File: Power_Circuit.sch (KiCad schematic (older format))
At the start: 34 parts, among them J1 Conn_01x09, J2 Conn_01x04, SW1 SW_Push, SW2 SW_STARTER, U1 B_Plug_Battery_In, U10 DSN2596, U11 B_Plug_12v_Motor1, U12 B_Plug_12v_Motor2, U13 B_Plug_5v_Actuator, U2 DSN2596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

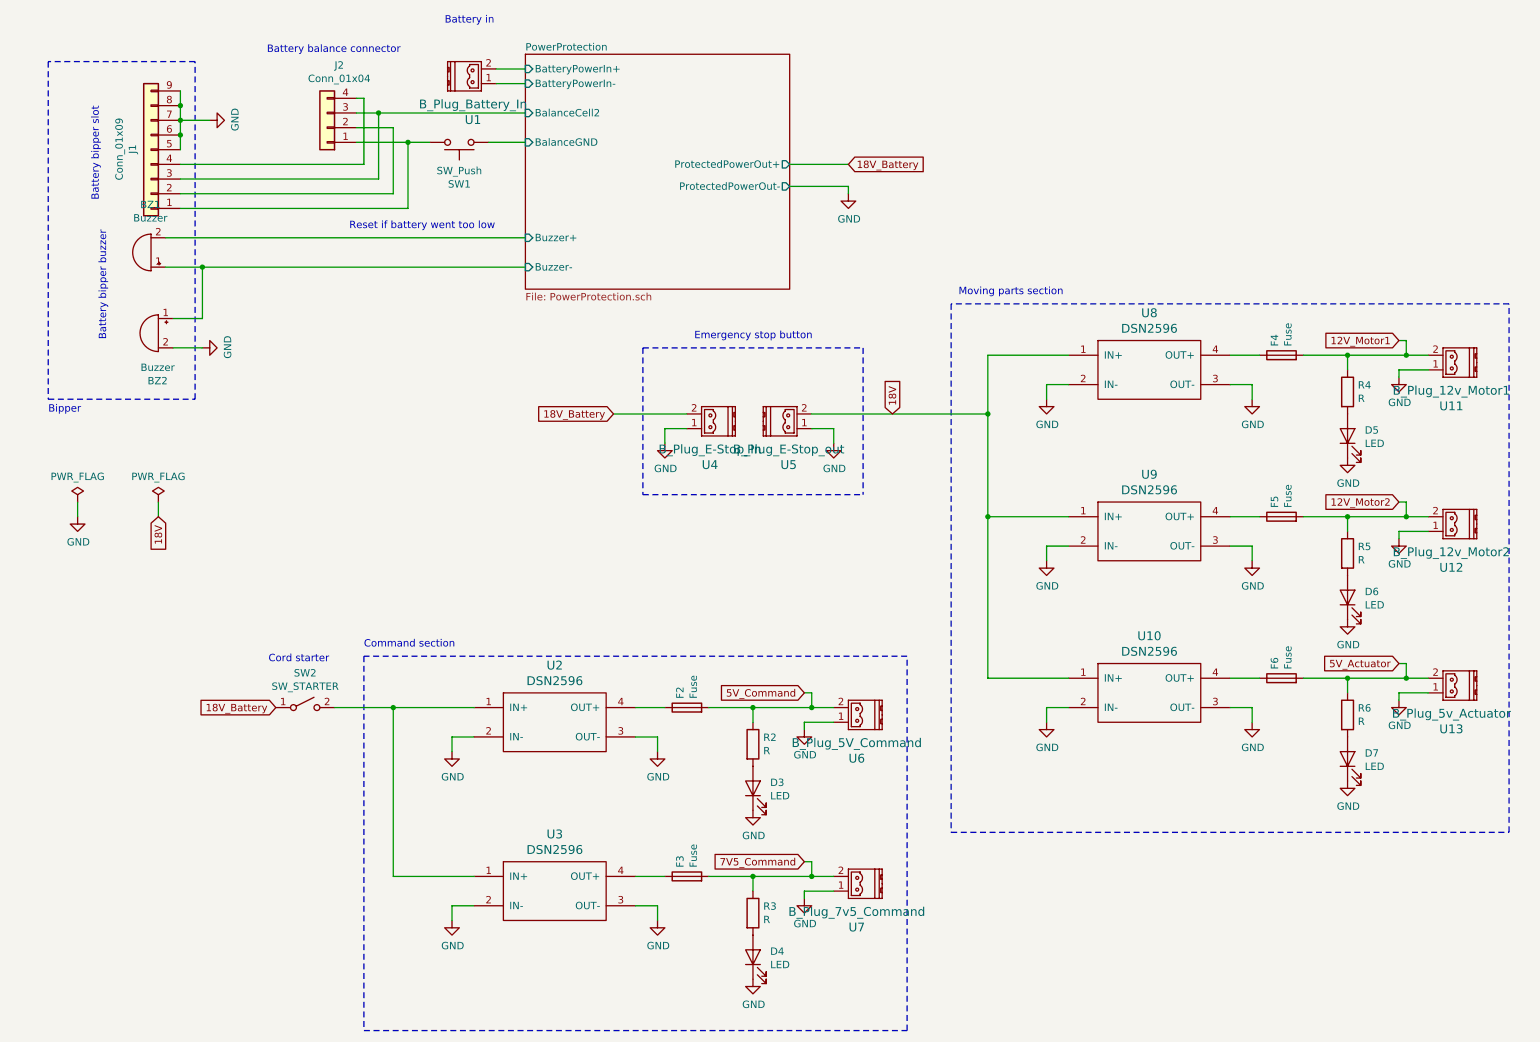
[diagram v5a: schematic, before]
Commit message: Avec regul moteur et texte sur autre couche
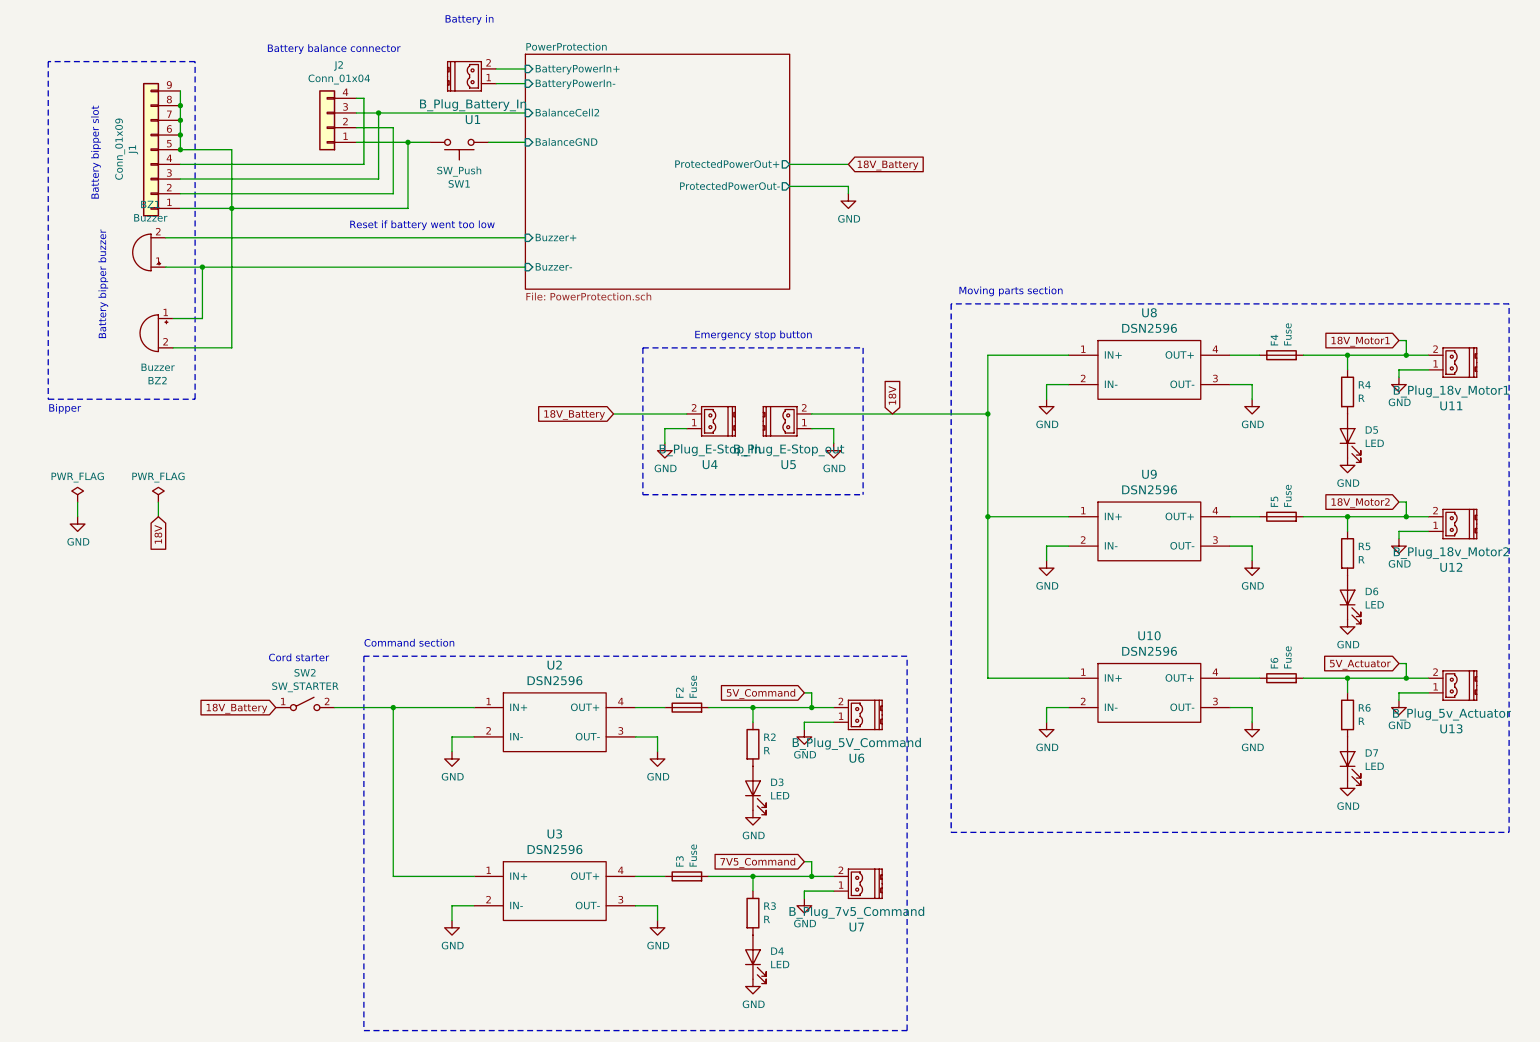
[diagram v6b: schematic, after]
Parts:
- U11: value B_Plug_12v_Motor1 -> B_Plug_18v_Motor1
- U12: value B_Plug_12v_Motor2 -> B_Plug_18v_Motor2
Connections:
- net GND: no longer BZ2.2 (+), J1.5 (Pin_5), J1.6 (Pin_6), J1.7 (Pin_7), J1.8 (Pin_8), J1.9 (Pin_9)
- net at J1.1 (Pin_1), J2.1 (Pin_1), SW1.2: now also BZ2.2 (+), J1.5 (Pin_5), J1.6 (Pin_6), J1.7 (Pin_7), J1.8 (Pin_8), J1.9 (Pin_9)
- net 12V_Motor1 renamed 18V_Motor1
- net 12V_Motor2 renamed 18V_Motor2
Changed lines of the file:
@@
 	6350 3600 6200 3600
-$Comp
-L dsn2596:DSN2596 U8
-U 1 1 5F54DB3F
-P 8500 3200
-F 0 "U8" H 8500 3587 60  0000 C CNN
-F 1 "DSN2596" H 8500 3481 60  0000 C CNN
-F 2 "DC_DC_LM2596_small:DC_DC_LM2596_small" H 8500 3200 60  0001 C CNN
-F 3 "" H 8500 3200 60  0000 C CNN
-	1    8500 3200
-	1    0    0    -1
-$EndComp
 $Comp
 L Device:R R4
@@
 $EndComp
 Wire Wire Line
-	9250 3100 9050 3100
-Wire Wire Line
 	9850 3100 9550 3100
 Connection ~ 9850 3100
-$Comp
-L power:GND #PWR018
-U 1 1 5F55577A
-P 9200 3400
-F 0 "#PWR018" H 9200 3150 50  0001 C CNN
-F 1 "GND" H 9205 3227 50  0000 C CNN
-F 2 "" H 9200 3400 50  0001 C CNN
-F 3 "" H 9200 3400 50  0001 C CNN
-	1    9200 3400
-	1    0    0    -1
-$EndComp
 $Comp
 L power:GND #PWR024
@@
 Wire Wire Line
 	10200 3200 10400 3200
-Wire Wire Line
-	9200 3400 9200 3300
-Wire Wire Line
-	9200 3300 9050 3300
 $Comp
 L 2:B_Plug_5mm U1
@@
 P 10500 3150
 F 0 "U11" H 10443 3447 60  0000 C CNN
-F 1 "B_Plug_12v_Motor1" H 10443 3341 60  0000 C CNN
+F 1 "B_Plug_18v_Motor1" H 10443 3341 60  0000 C CNN
 F 2 "Connector_Phoenix_MC:PhoenixContact_MCV_1,5_2-G-3.81_1x02_P3.81mm_Vertical" H 10500 3150 60  0001 C CNN
 F 3 "" H 10500 3150 60  0000 C CNN
 	1    10500 3150
 	-1   0    0    1
-$EndComp
-$Comp
-L power:GND #PWR015
-U 1 1 5F562803
-P 7800 3400
-F 0 "#PWR015" H 7800 3150 50  0001 C CNN
-F 1 "GND" H 7805 3227 50  0000 C CNN
-F 2 "" H 7800 3400 50  0001 C CNN
-F 3 "" H 7800 3400 50  0001 C CNN
-	1    7800 3400
-	1    0    0    -1
-$EndComp
-Wire Wire Line
-	7800 3400 7800 3300
-Wire Wire Line
-	7950 3300 7800 3300
-$Comp
-L dsn2596:DSN2596 U9
-U 1 1 5F568932
-P 8500 4300
-F 0 "U9" H 8500 4687 60  0000 C CNN
-F 1 "DSN2596" H 8500 4581 60  0000 C CNN
-F 2 "DC_DC_LM2596_small:DC_DC_LM2596_small" H 8500 4300 60  0001 C CNN
-F 3 "" H 8500 4300 60  0000 C CNN
-	1    8500 4300
-	1    0    0    -1
 $EndComp
 $Comp
@@
 $EndComp
 Wire Wire Line
-	9250 4200 9050 4200
-Wire Wire Line
 	9850 4200 9550 4200
 Connection ~ 9850 4200
-$Comp
-L power:GND #PWR019
-U 1 1 5F568954
-P 9200 4500
-F 0 "#PWR019" H 9200 4250 50  0001 C CNN
-F 1 "GND" H 9205 4327 50  0000 C CNN
-F 2 "" H 9200 4500 50  0001 C CNN
-F 3 "" H 9200 4500 50  0001 C CNN
-	1    9200 4500
-	1    0    0    -1
-$EndComp
 $Comp
 L power:GND #PWR025
@@
 Wire Wire Line
 	9850 4200 10250 4200
-Wire Wire Line
-	9200 4500 9200 4400
-Wire Wire Line
-	9200 4400 9050 4400
 $Comp
 L 2:B_Plug_5mm U12
@@
 P 10500 4250
 F 0 "U12" H 10443 4547 60  0000 C CNN
-F 1 "B_Plug_12v_Motor2" H 10443 4441 60  0000 C CNN
+F 1 "B_Plug_18v_Motor2" H 10443 4441 60  0000 C CNN
 F 2 "Connector_Phoenix_MC:PhoenixContact_MCV_1,5_2-G-3.81_1x02_P3.81mm_Vertical" H 10500 4250 60  0001 C CNN
 F 3 "" H 10500 4250 60  0000 C CNN
@@
 	-1   0    0    1
 $EndComp
-$Comp
-L power:GND #PWR016
-U 1 1 5F56896B
-P 7800 4500
-F 0 "#PWR016" H 7800 4250 50  0001 C CNN
-F 1 "GND" H 7805 4327 50  0000 C CNN
-F 2 "" H 7800 4500 50  0001 C CNN
-F 3 "" H 7800 4500 50  0001 C CNN
-	1    7800 4500
-	1    0    0    -1
-$EndComp
-Wire Wire Line
-	7800 4500 7800 4400
-Wire Wire Line
-	7950 4400 7800 4400
-Wire Wire Line
-	7950 4200 7400 4200
 $Comp
 L dsn2596:DSN2596 U10
@@
 Wire Wire Line
 	7950 5300 7400 5300
-Connection ~ 7400 4200
 Wire Wire Line
 	6200 3500 7400 3500
-Wire Wire Line
-	7400 3500 7400 4200
-Wire Wire Line
-	7400 4200 7400 5300
 Wire Notes Line
 	5050 4050 6550 4050
@@
 Wire Notes Line
 	5050 3050 6550 3050
-Text GLabel 10200 4100 0    50   Input ~ 0
-12V_Motor2
 Text GLabel 10200 5200 0    50   Input ~ 0
 5V_Actuator
@@
 Wire Wire Line
 	3900 5700 3750 5700
-Wire Wire Line
-	3900 5500 3350 5500
 Text GLabel 6150 5400 0    50   Input ~ 0
 5V_Command
@@
 Wire Notes Line
 	10950 6350 10950 2750
-Wire Notes Line
-	10950 2750 7150 2750
 Wire Notes Line
 	5050 3050 5050 4050
@@
 $EndComp
 Wire Wire Line
-	1900 2100 3450 2100
+	1900 2100 2250 2100
 Wire Wire Line
 	1900 1900 3250 1900
@@
 Wire Wire Line
 	6450 1950 6050 1950
-$Comp
-L power:GND #PWR02
-U 1 1 5FA54FE4
-P 2100 1500
-F 0 "#PWR02" H 2100 1250 50  0001 C CNN
-F 1 "GND" H 2105 1327 50  0000 C CNN
-F 2 "" H 2100 1500 50  0001 C CNN
-F 3 "" H 2100 1500 50  0001 C CNN
-	1    2100 1500
-	0    -1   -1   0
-$EndComp
-Wire Wire Line
-	2100 1500 1900 1500
 Wire Notes Line
 	1000 1100 1000 3400
@@
 Wire Wire Line
 	10250 3000 10250 3100
-Text GLabel 10200 3000 0    50   Input ~ 0
-12V_Motor1
 Wire Wire Line
 	10200 5400 10200 5450
@@
 Wire Wire Line
 	1200 4100 1200 4200
-Wire Wire Line
-	7950 3100 7400 3100
 $Comp
 L power:PWR_FLAG #FLG0102
@@
 Wire Wire Line
 	2050 2850 1850 2850
-$Comp
-L power:GND #PWR0103
-U 1 1 5FB650C4
-P 2050 3050
-F 0 "#PWR0103" H 2050 2800 50  0001 C CNN
-F 1 "GND" H 2055 2877 50  0000 C CNN
-F 2 "" H 2050 3050 50  0001 C CNN
-F 3 "" H 2050 3050 50  0001 C CNN
-	1    2050 3050
-	0    -1   -1   0
-$EndComp
-Wire Wire Line
-	2050 3050 1850 3050
 Wire Wire Line
 	2050 2850 2050 2500
@@
 Wire Wire Line
 	2050 2500 4250 2500
+Text GLabel 10200 4100 0    50   Input ~ 0
+18V_Motor2
+Text GLabel 10200 3000 0    50   Input ~ 0
+18V_Motor1
+Wire Wire Line
+	3900 5500 3350 5500
+Wire Wire Line
+	2250 2100 2250 3050
+Connection ~ 2250 2100
+Wire Wire Line
+	2250 2100 3450 2100
+Wire Wire Line
+	1850 3050 2250 3050
+Wire Wire Line
+	1900 1700 2250 1700
+Wire Wire Line
+	2250 1700 2250 2100
+Connection ~ 1900 1700
+Wire Wire Line
+	7400 3500 7400 4200
+Wire Notes Line
+	10950 2750 7150 2750
+$Comp
+L dsn2596:DSN2596 U9
+U 1 1 5FAB91D9
+P 8500 4300
+F 0 "U9" H 8500 4687 60  0000 C CNN
+F 1 "DSN2596" H 8500 4581 60  0000 C CNN
+F 2 "DC_DC_LM2596_small:DC_DC_LM2596_small" H 8500 4300 60  0001 C CNN
+F 3 "" H 8500 4300 60  0000 C CNN
+	1    8500 4300
+	1    0    0    -1
+$EndComp
+$Comp
+L power:GND #PWR0102
+U 1 1 5FAB91DF
+P 9200 4500
+F 0 "#PWR0102" H 9200 4250 50  0001 C CNN
+F 1 "GND" H 9205 4327 50  0000 C CNN
+F 2 "" H 9200 4500 50  0001 C CNN
+F 3 "" H 9200 4500 50  0001 C CNN
+	1    9200 4500
+	1    0    0    -1
+$EndComp
+Wire Wire Line
+	9200 4500 9200 4400
+Wire Wire Line
+	9200 4400 9050 4400
+$Comp
+L power:GND #PWR0103
+U 1 1 5FAB91E7
+P 7800 4500
+F 0 "#PWR0103" H 7800 4250 50  0001 C CNN
+F 1 "GND" H 7805 4327 50  0000 C CNN
+F 2 "" H 7800 4500 50  0001 C CNN
+F 3 "" H 7800 4500 50  0001 C CNN
+	1    7800 4500
+	1    0    0    -1
+$EndComp
+Wire Wire Line
+	7800 4500 7800 4400
+Wire Wire Line
+	7950 4400 7800 4400
+$Comp
+L dsn2596:DSN2596 U8
+U 1 1 5FABDC55
+P 8500 3200
+F 0 "U8" H 8500 3587 60  0000 C CNN
+F 1 "DSN2596" H 8500 3481 60  0000 C CNN
+F 2 "DC_DC_LM2596_small:DC_DC_LM2596_small" H 8500 3200 60  0001 C CNN
+F 3 "" H 8500 3200 60  0000 C CNN
+	1    8500 3200
+	1    0    0    -1
+$EndComp
+$Comp
+L power:GND #PWR0105
+U 1 1 5FABDC5B
+P 9200 3400
+F 0 "#PWR0105" H 9200 3150 50  0001 C CNN
+F 1 "GND" H 9205 3227 50  0000 C CNN
+F 2 "" H 9200 3400 50  0001 C CNN
+F 3 "" H 9200 3400 50  0001 C CNN
+	1    9200 3400
+	1    0    0    -1
+$EndComp
+Wire Wire Line
+	9200 3400 9200 3300
+Wire Wire Line
+	9200 3300 9050 3300
+$Comp
+L power:GND #PWR0107
+U 1 1 5FABDC63
+P 7800 3400
+F 0 "#PWR0107" H 7800 3150 50  0001 C CNN
+F 1 "GND" H 7805 3227 50  0000 C CNN
+F 2 "" H 7800 3400 50  0001 C CNN
+F 3 "" H 7800 3400 50  0001 C CNN
+	1    7800 3400
+	1    0    0    -1
+$EndComp
+Wire Wire Line
+	7800 3400 7800 3300
+Wire Wire Line
+	7950 3300 7800 3300
+Wire Wire Line
+	9250 3100 9050 3100
+Wire Wire Line
+	7950 3100 7400 3100
+Wire Wire Line
+	7950 4200 7400 4200
+Connection ~ 7400 4200
+Wire Wire Line
+	7400 4200 7400 5300
+Wire Wire Line
+	9250 4200 9050 4200
 $EndSCHEMATC

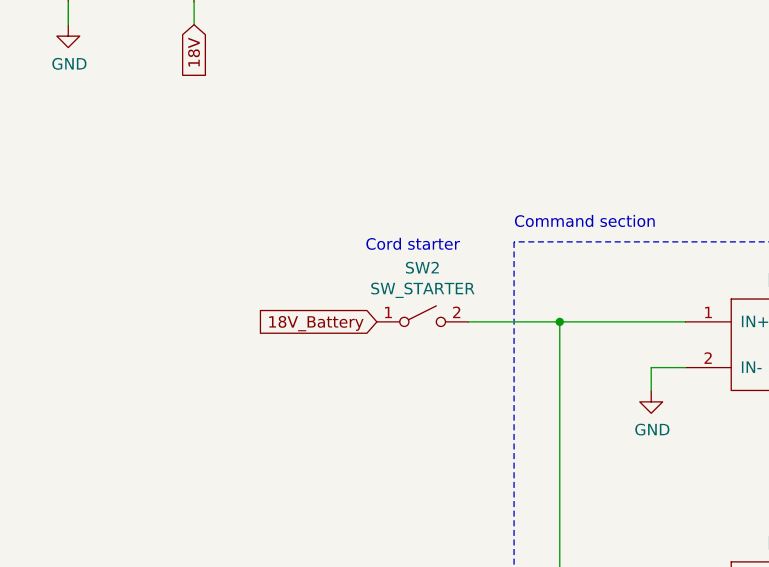
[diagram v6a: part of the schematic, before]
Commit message: Ajout BOM, suppression tirette, correction silk, correction des plans pour meilleur refroidissement du transistor notamment
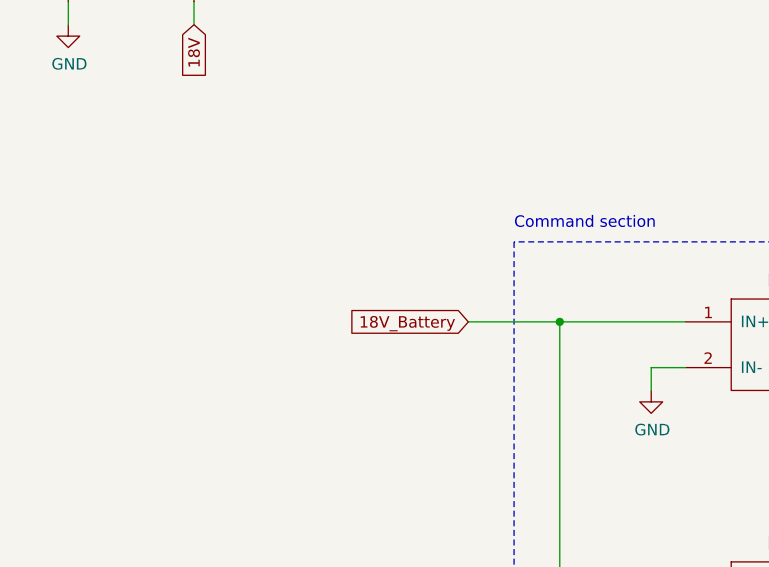
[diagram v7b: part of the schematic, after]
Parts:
- removed SW2: SW_STARTER, LIB_BE_PHELMA:R_Axial_DIN0207_L6.3mm_D2.5mm_P10.16mm_Horizontal, symbol Switch:SW_SPST
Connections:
- net 18V_Battery: now also U2.1 (IN+), U3.1 (IN+)
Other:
- note removed: "Cord starter"
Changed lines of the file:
@@
 Text GLabel 4850 3500 0    50   Input ~ 0
 18V_Battery
-Text GLabel 2550 5500 0    50   Input ~ 0
+Text GLabel 2950 5500 0    50   Input ~ 0
 18V_Battery
 Wire Wire Line
@@
 	1800 2500 2050 2500
 $Comp
-L Switch:SW_SPST SW2
-U 1 1 5F8A3132
-P 2750 5500
-F 0 "SW2" H 2750 5735 50  0000 C CNN
-F 1 "SW_STARTER" H 2750 5644 50  0000 C CNN
-F 2 "LIB_BE_PHELMA:R_Axial_DIN0207_L6.3mm_D2.5mm_P10.16mm_Horizontal" H 2750 5500 50  0001 C CNN
-F 3 "~" H 2750 5500 50  0001 C CNN
-	1    2750 5500
-	1    0    0    -1
-$EndComp
-Text Notes 2500 5200 0    50   ~ 0
-Cord starter
-$Comp
 L Device:Buzzer BZ2
